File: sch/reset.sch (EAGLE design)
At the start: 17 parts, among them IC1 74LS123N, IC2 74LS14N, IC3 74LS74N, IC4 74LS132N, IC5 74LS32N, IC6 74LS373N

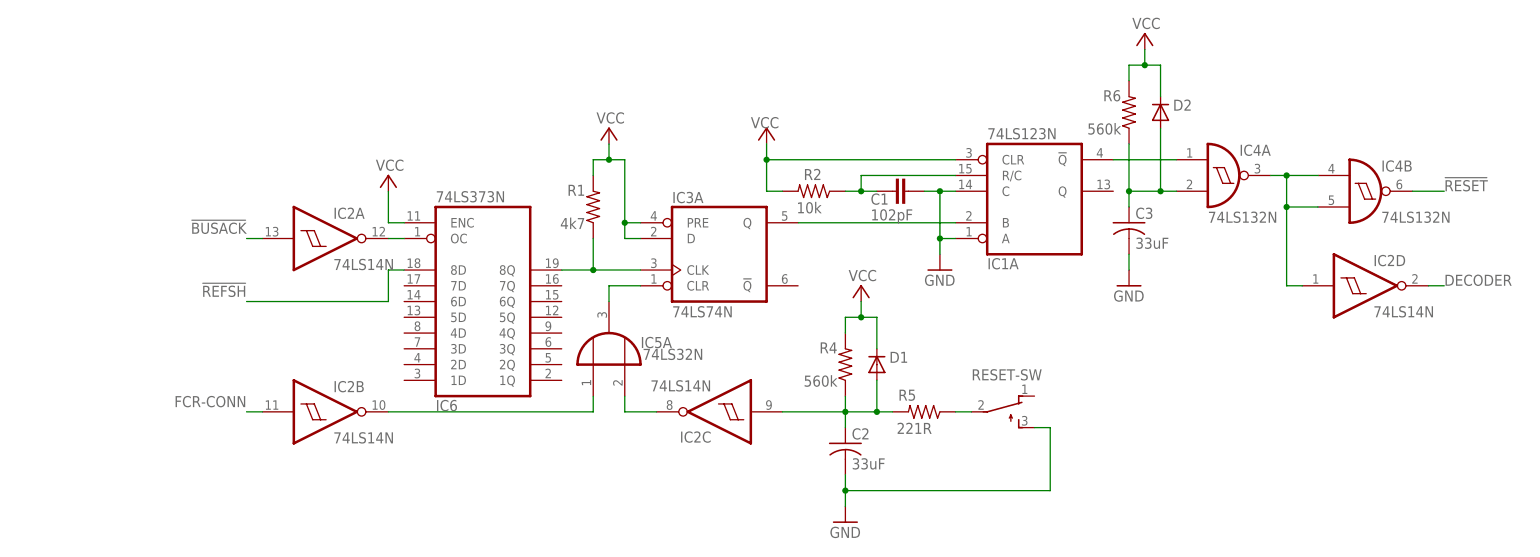
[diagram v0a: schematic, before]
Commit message: Removed redundant buffer from the reset schematic.
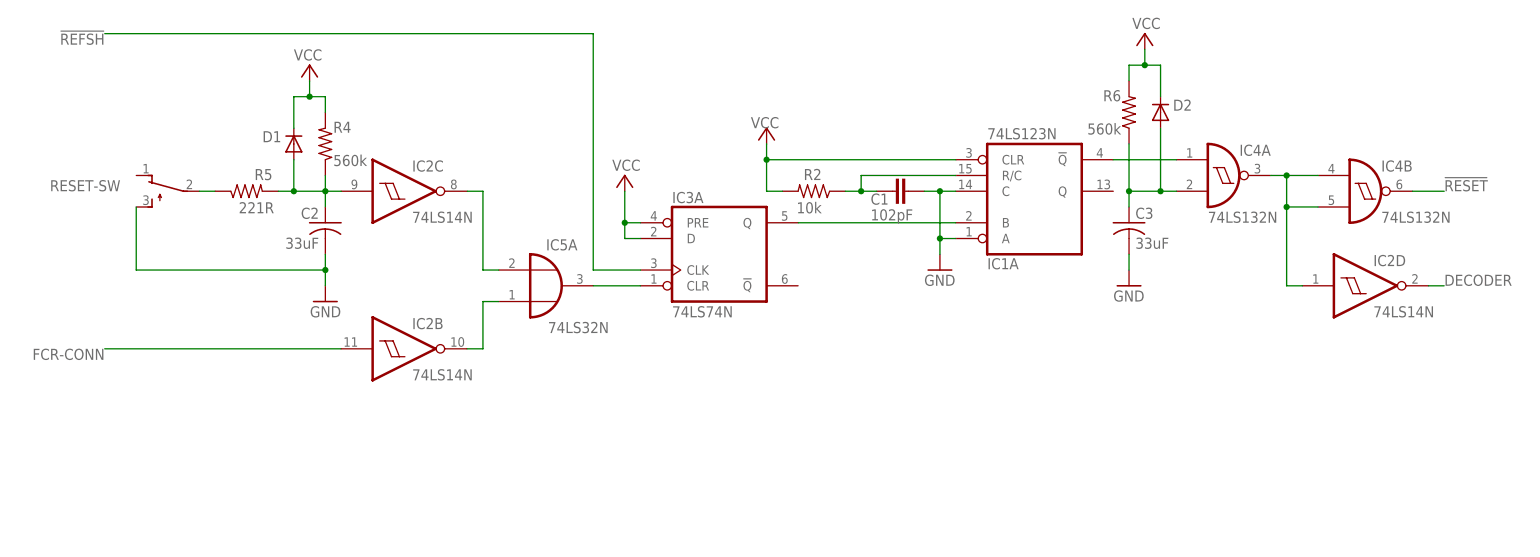
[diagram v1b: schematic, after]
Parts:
- removed IC6: 74LS373N, 74xx-eu:74LS373N
- removed R1: 4k7, resistor:R-US_0204/7
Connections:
- removed net !BUSACK!: IC2A.I
- removed net N$1: IC2A.O, IC6A.OC
- removed net N$2: IC3A.CLK, IC6A.8Q, R1.1
- net !REFSH!: now also IC3A.CLK; no longer IC6A.8D
- net VCC: no longer IC6A.ENC, R1.2
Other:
- moved on the sheet: C2, D1, IC2B, IC2C, IC5A, R4, R5, RESET-SW
